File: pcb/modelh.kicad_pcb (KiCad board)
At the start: 2 copper layers, 150 x 38 mm, 51 parts, among them J1 USB_B, J2 Conn_cols, J3 Conn_rows, J4 Conn_leds, J5 Conn_02x03_Odd_Even, J6 Conn_02x05_Odd_Even, J7 Conn_01x05, J8 Conn_01x05, J9 Conn_01x05, SW1 SW_Push, U1 STM32F103C8Tx, U2 AMS1117-3.3, Y1 8MHz

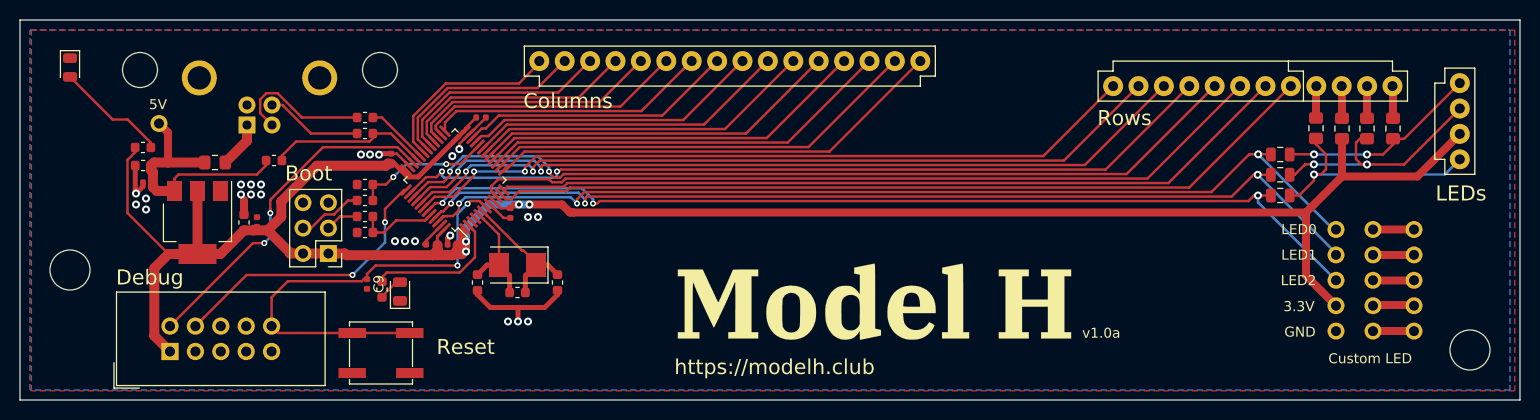
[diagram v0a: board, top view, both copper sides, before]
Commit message: ground stitching
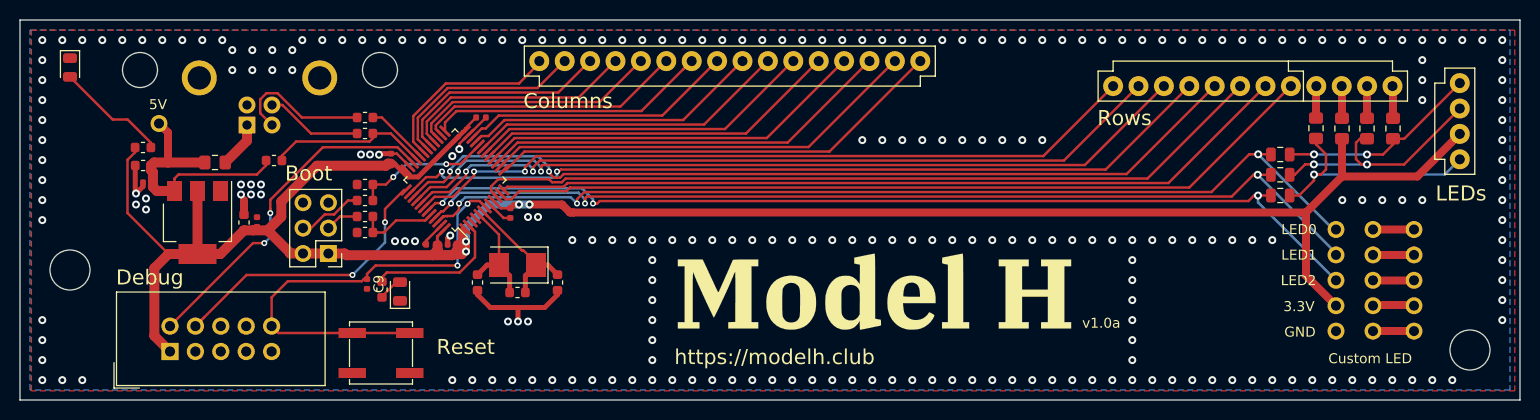
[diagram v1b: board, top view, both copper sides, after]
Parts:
- moved G*** 1.00 mm to (150.2, 74.2)
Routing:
- net GND: vias 23 -> 248

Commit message: nearly done
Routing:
- net +3V3: track 228.4 -> 229.5 mm
- net col1: vias 1 -> 0
- net GND: vias 248 -> 272
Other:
- board text added: "Boot0"
- board text added: "Boot1"
- board text removed: "Boot"

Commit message: WIP
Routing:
- net GND: vias 272 -> 271
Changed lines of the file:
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@@
     (thickness 1.6)
     (drawings 30)
-    (tracks 817)
+    (tracks 816)
     (zones 0)
     (modules 51)
@@
   (via (at 83 83) (size 0.8) (drill 0.4) (layers F.Cu B.Cu) (net 1))
   (via (at 73 83) (size 0.8) (drill 0.4) (layers F.Cu B.Cu) (net 1))
-  (via (at 75 83) (size 0.8) (drill 0.4) (layers F.Cu B.Cu) (net 1))
   (via (at 77 83) (size 0.8) (drill 0.4) (layers F.Cu B.Cu) (net 1))
   (via (at 79 83) (size 0.8) (drill 0.4) (layers F.Cu B.Cu) (net 1))

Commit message: WIP
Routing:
- net GND: vias 271 -> 268
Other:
- outline, holes or cut-outs redrawn
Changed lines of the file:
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@@
   (general
     (thickness 1.6)
-    (drawings 30)
-    (tracks 816)
+    (drawings 34)
+    (tracks 813)
     (zones 0)
     (modules 51)
@@
   )
   (setup
-    (last_trace_width 0.8)
+    (last_trace_width 0.25)
     (user_trace_width 0.3)
     (user_trace_width 0.5)
@@
     (solder_mask_min_width 0.101)
     (aux_axis_origin 64.77 46.99)
+    (grid_origin 64.77 46.99)
     (visible_elements FFFFFF7F)
     (pcbplotparams
@@
     (tags capacitor)
     (attr smd)
-    (fp_text reference C9 (at 0 -1.17 90) (layer F.SilkS)
+    (fp_text reference C9 (at 0 -1.17 90) (layer F.Fab)
       (effects (font (size 1 1) (thickness 0.15)))
     )
@@
       (zone_connect 0))
   )
+  (gr_arc (start 211.77 49.99) (end 214.77 49.99) (angle -90) (layer Edge.Cuts) (width 0.001))
+  (gr_arc (start 211.77 81.99) (end 211.77 84.99) (angle -90) (layer Edge.Cuts) (width 0.001))
+  (gr_arc (start 67.77 81.99) (end 64.77 81.99) (angle -90) (layer Edge.Cuts) (width 0.001))
+  (gr_arc (start 67.77 49.99) (end 67.77 46.99) (angle -90) (layer Edge.Cuts) (width 0.001))
   (gr_text Boot1 (at 99.8 70.3) (layer F.SilkS)
     (effects (font (size 1 1) (thickness 0.15)))
@@
     (arrow2b (pts (xy 64.77 40.49) (xy 65.896504 39.903579)))
   )
-  (gr_line (start 64.77 84.99) (end 64.77 46.99) (layer Edge.Cuts) (width 0.001))
-  (gr_line (start 214.77 84.99) (end 64.77 84.99) (layer Edge.Cuts) (width 0.001))
-  (gr_line (start 214.77 46.99) (end 214.77 84.99) (layer Edge.Cuts) (width 0.001))
-  (gr_line (start 64.77 46.99) (end 214.77 46.99) (layer Edge.Cuts) (width 0.001))
+  (gr_line (start 64.77 81.99) (end 64.77 49.99) (layer Edge.Cuts) (width 0.001))
+  (gr_line (start 211.77 84.99) (end 67.77 84.99) (layer Edge.Cuts) (width 0.001))
+  (gr_line (start 214.77 49.99) (end 214.77 81.99) (layer Edge.Cuts) (width 0.001))
+  (gr_line (start 67.77 46.99) (end 211.77 46.99) (layer Edge.Cuts) (width 0.001))
   (dimension 38 (width 0.12) (layer Dwgs.User)
     (gr_text "38.000 mm" (at 42 65.99 270) (layer Dwgs.User)
@@
   (via (at 213 53) (size 0.8) (drill 0.4) (layers F.Cu B.Cu) (net 1))
   (via (at 213 51) (size 0.8) (drill 0.4) (layers F.Cu B.Cu) (net 1))
-  (via (at 213 49) (size 0.8) (drill 0.4) (layers F.Cu B.Cu) (net 1))
   (via (at 148 83) (size 0.8) (drill 0.4) (layers F.Cu B.Cu) (net 1))
   (via (at 170 83) (size 0.8) (drill 0.4) (layers F.Cu B.Cu) (net 1))
@@
   (via (at 202 83) (size 0.8) (drill 0.4) (layers F.Cu B.Cu) (net 1))
   (via (at 204 83) (size 0.8) (drill 0.4) (layers F.Cu B.Cu) (net 1))
-  (via (at 67 83) (size 0.8) (drill 0.4) (layers F.Cu B.Cu) (net 1))
   (via (at 69 83) (size 0.8) (drill 0.4) (layers F.Cu B.Cu) (net 1))
   (via (at 71 83) (size 0.8) (drill 0.4) (layers F.Cu B.Cu) (net 1))
@@
   (via (at 67 79) (size 0.8) (drill 0.4) (layers F.Cu B.Cu) (net 1))
   (via (at 67 77) (size 0.8) (drill 0.4) (layers F.Cu B.Cu) (net 1))
-  (via (at 67 49) (size 0.8) (drill 0.4) (layers F.Cu B.Cu) (net 1))
   (via (at 67 51) (size 0.8) (drill 0.4) (layers F.Cu B.Cu) (net 1))
   (via (at 67 53) (size 0.8) (drill 0.4) (layers F.Cu B.Cu) (net 1))
@@
   (segment (start 208.76 53.3) (end 203.195 58.865) (width 0.25) (layer F.Cu) (net 5))
   (segment (start 208.77 53.3) (end 208.76 53.3) (width 0.25) (layer F.Cu) (net 5))
+  (segment (start 77.8575 59.74) (end 77.8575 59.265) (width 0.25) (layer F.Cu) (net 6))
+  (segment (start 77.8575 59.265) (end 75.5325 56.94) (width 0.25) (layer F.Cu) (net 6))
+  (segment (start 75.5325 56.94) (end 74.0325 56.94) (width 0.25) (layer F.Cu) (net 6))
+  (segment (start 74.0325 56.94) (end 69.77 52.6775) (width 0.25) (layer F.Cu) (net 6))
   (segment (start 91.02 55.49) (end 89.97 55.49) (width 0.25) (layer F.Cu) (net 7))
   (segment (start 93.87 58.34) (end 91.02 55.49) (width 0.25) (layer F.Cu) (net 7))
@@
   (segment (start 108.033552 70.51001) (end 108.974672 70.51001) (width 0.8) (layer F.Cu) (net 9))
   (segment (start 76.2825 59.74) (end 76.2825 60.215) (width 0.25) (layer F.Cu) (net 9))
-  (segment (start 77.8575 59.74) (end 77.8575 59.265) (width 0.25) (layer F.Cu) (net 6))
-  (segment (start 77.8575 59.265) (end 75.5325 56.94) (width 0.25) (layer F.Cu) (net 6))
-  (segment (start 75.5325 56.94) (end 74.0325 56.94) (width 0.25) (layer F.Cu) (net 6))
-  (segment (start 74.0325 56.94) (end 69.77 52.6775) (width 0.25) (layer F.Cu) (net 6))
   (segment (start 193.37 72.56) (end 196.37 75.56) (width 0.8) (layer F.Cu) (net 9))
   (segment (start 193.37 66.24) (end 193.37 72.56) (width 0.8) (layer F.Cu) (net 9))
@@
     (connect_pads yes (clearance 0.5))
     (min_thickness 0.254)
-    (fill yes (arc_segments 32) (thermal_gap 0.508) (thermal_bridge_width 0.508))
+    (fill yes (arc_segments 32) (thermal_gap 0.508) (thermal_bridge_width 0.508) (smoothing fillet) (radius 2))
     (polygon
       (pts
-        (xy 214.246 84.074) (xy 65.91 84.074) (xy 65.91 48.006) (xy 214.246 48.006)
+        (xy 213.77 83.99) (xy 65.77 83.99) (xy 65.77 47.99) (xy 213.77 47.99)
       )
     )
@@
     (connect_pads (clearance 0.508))
     (min_thickness 0.254)
-    (fill yes (arc_segments 32) (thermal_gap 0.508) (thermal_bridge_width 0.508))
+    (fill yes (arc_segments 32) (thermal_gap 0.508) (thermal_bridge_width 0.508) (smoothing fillet) (radius 2))
     (polygon
       (pts
